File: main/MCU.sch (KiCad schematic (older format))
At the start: 16 parts, among them U2 EFM32GG990F1024

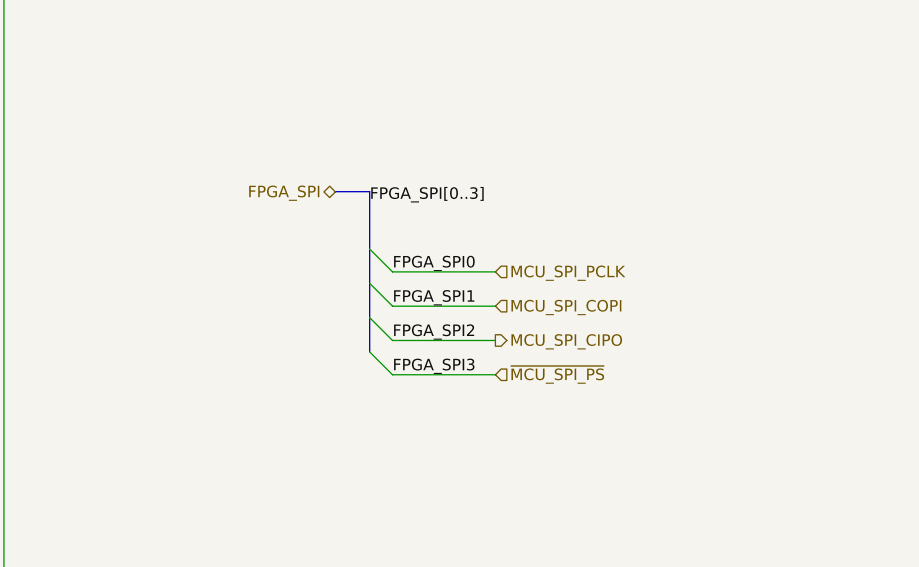
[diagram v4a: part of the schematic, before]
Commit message: Simplify the top sheet, put bus connection inside the sheets
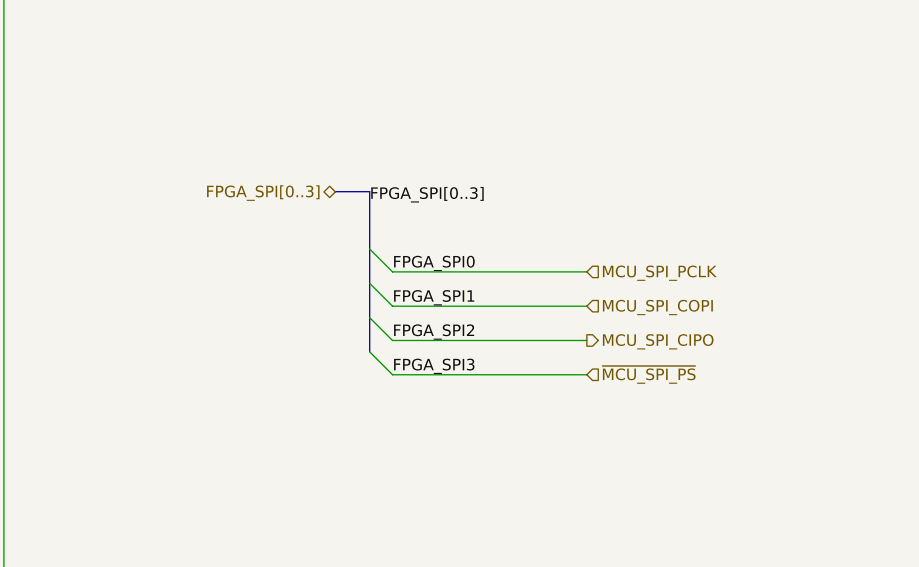
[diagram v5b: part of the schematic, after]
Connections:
- net labels removed: FPGA_SPI
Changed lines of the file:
@@
 Entry Wire Line
 	7700 3550 7800 3650
-Text HLabel 8250 4100 2    50   Input ~ 0
+Text HLabel 8650 4100 2    50   Input ~ 0
 ~MCU_SPI_PS
-Text HLabel 8250 3950 2    50   Output ~ 0
+Text HLabel 8650 3950 2    50   Output ~ 0
 MCU_SPI_CIPO
-Text HLabel 8250 3800 2    50   Input ~ 0
+Text HLabel 8650 3800 2    50   Input ~ 0
 MCU_SPI_COPI
-Text HLabel 8250 3650 2    50   Input ~ 0
+Text HLabel 8650 3650 2    50   Input ~ 0
 MCU_SPI_PCLK
 Text Label 7700 3350 0    50   ~ 0
@@
 FPGA_SPI3
 Wire Wire Line
-	7800 3650 8250 3650
+	7800 3650 8650 3650
 Wire Wire Line
-	7800 3800 8250 3800
+	7800 3800 8650 3800
 Wire Wire Line
-	7800 3950 8250 3950
+	7800 3950 8650 3950
 Wire Wire Line
-	7800 4100 8250 4100
+	7800 4100 8650 4100
 Wire Bus Line
 	7700 3300 7550 3300
 Text HLabel 7550 3300 0    50   BiDi ~ 0
-FPGA_SPI
+FPGA_SPI[0..3]
 Text Label 7800 3650 0    50   ~ 0
 FPGA_SPI0

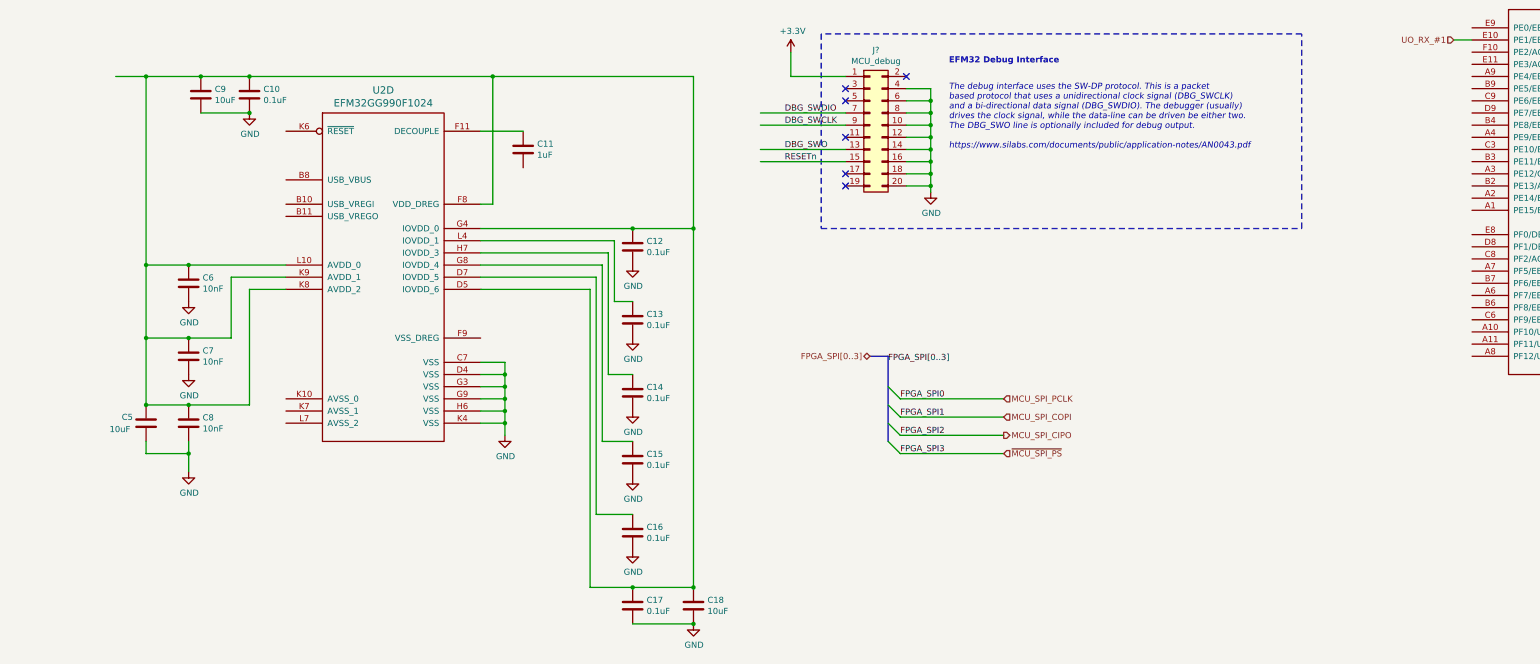
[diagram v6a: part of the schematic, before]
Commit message: Finish (?) setting up FPGA as in the slides
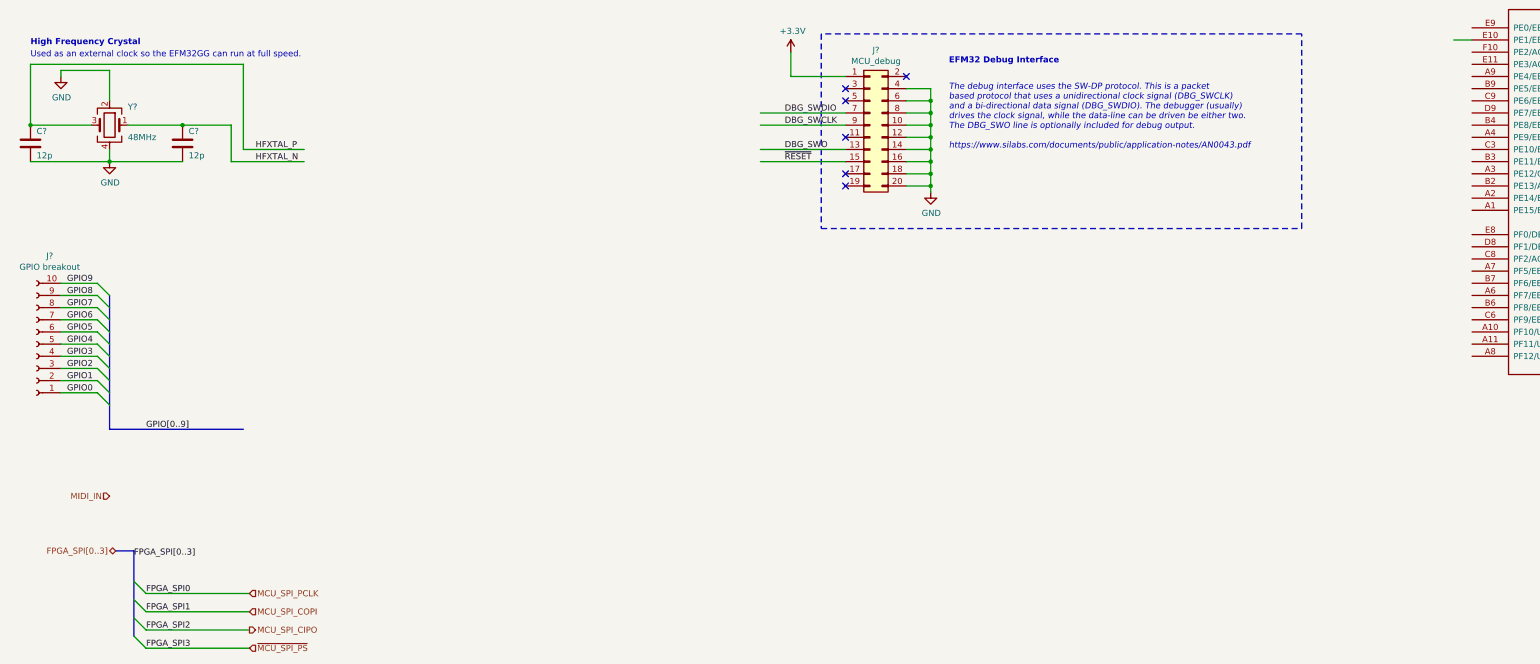
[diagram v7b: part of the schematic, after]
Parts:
- removed C10, C12, C13, C14, C15, C16, C17: 0.1uF, symbol Device:C
- removed C11: 1uF, symbol Device:C
- removed C18, C5, C9: 10uF, symbol Device:C
- removed C6, C7, C8: 10nF, symbol Device:C
- removed unit 4 of U2
- added C? (x2): 12p, symbol Device:C
- added J?: GPIO breakout, symbol Connector:Conn_01x10_Female
- added Y?: 48MHz, symbol Device:Crystal_GND24
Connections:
- net labels added: GPIO0, GPIO1, GPIO2, GPIO3, GPIO4, GPIO5, GPIO6, GPIO7, GPIO8, GPIO9, GPIO[0..9], HFXTAL_N, HFXTAL_P, MIDI_IN, ~RESET
- net labels removed: RESETn, UO_RX_#1
- wire segments 88 -> 54
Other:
- note added: "High Frequency Crystal"
- note added: "Used as an external clock so the EFM32GG can run at full speed."

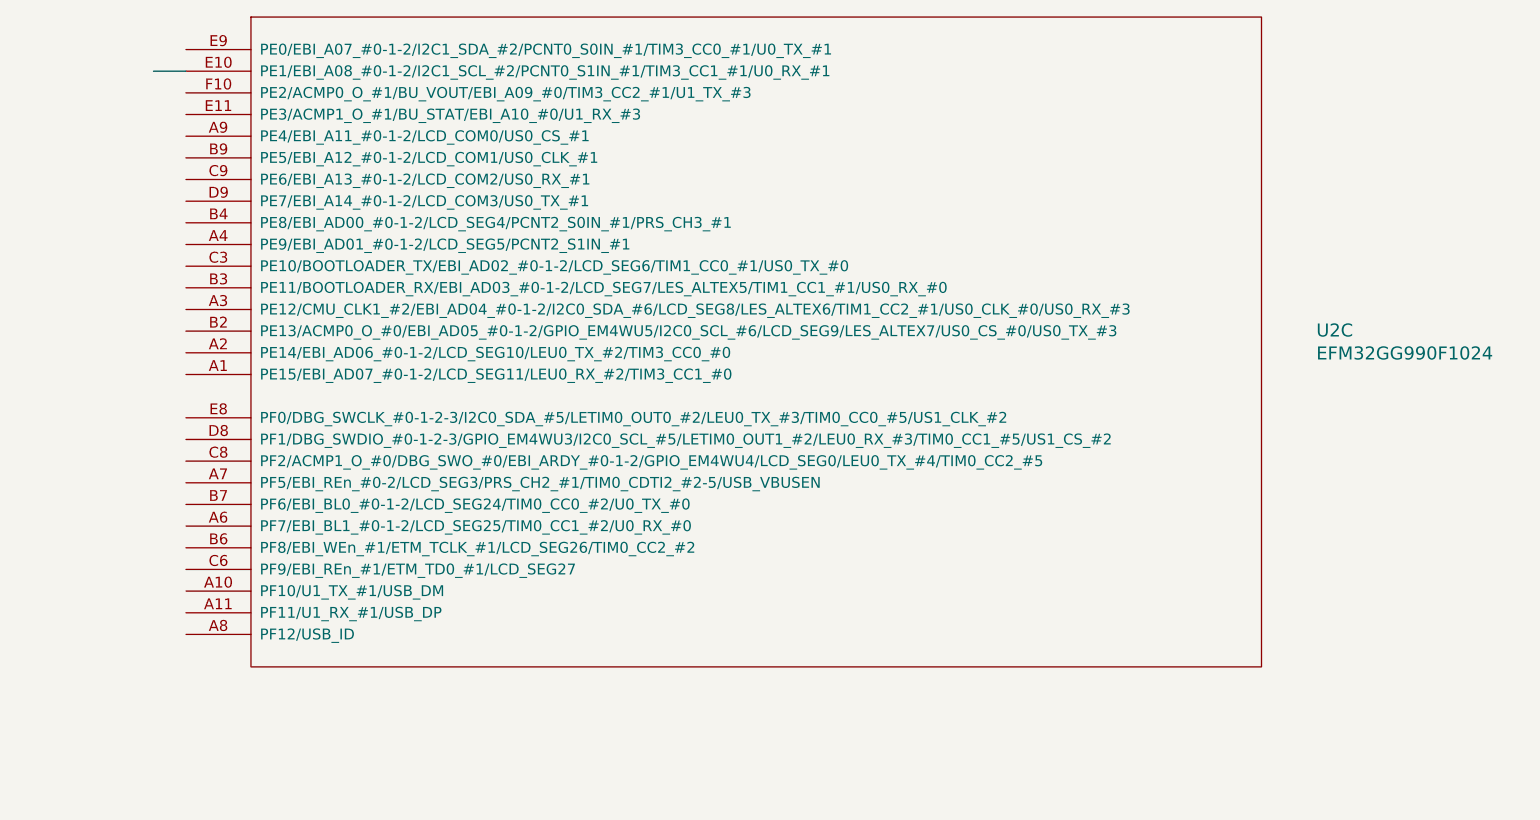
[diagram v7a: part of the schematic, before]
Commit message: Add FPGA oscillator, cleanup
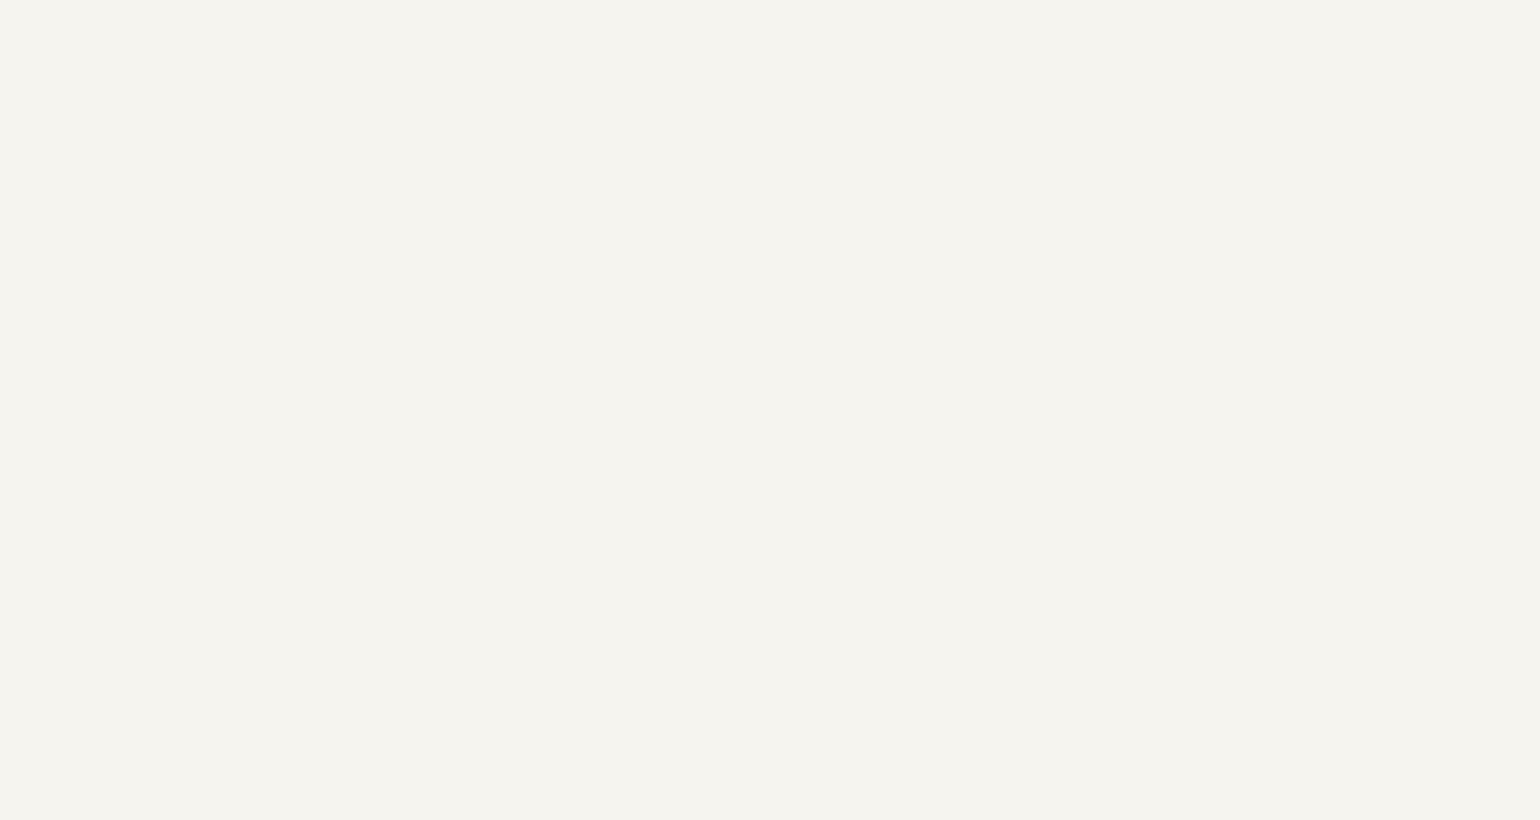
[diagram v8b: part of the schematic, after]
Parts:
- removed U2: EFM32GG990F1024, symbol energymicro-efm32:EFM32GG990F1024
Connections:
- wire segments 54 -> 53
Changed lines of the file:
@@
 Comment4 ""
 $EndDescr
-$Comp
-L energymicro-efm32:EFM32GG990F1024 U2
-U 3 1 613D4762
-P 12500 600
-F 0 "U2" H 17718 -697 60  0000 L CNN
-F 1 "EFM32GG990F1024" H 17718 -803 60  0000 L CNN
-F 2 "" H 12500 600 50  0001 C CNN
-F 3 "http://www.energymicro.com/downloads/datasheets" H 12500 600 50  0001 C CNN
-	3    12500 600
-	1    0    0    -1
-$EndComp
 Text HLabel 1300 4450 0    50   Input ~ 0
 MIDI_IN
-Wire Wire Line
-	12350 700  12500 700
 Entry Wire Line
 	1500 5600 1600 5700
